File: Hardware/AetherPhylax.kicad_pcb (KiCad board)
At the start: 2 copper layers, 35 x 38 mm, 39 parts, among them J1 Conn_01x01_Pin, J2 Conn_01x01_Pin, U2 BME280, U3 STM32G071KxU, U4 RFM95W-868S2

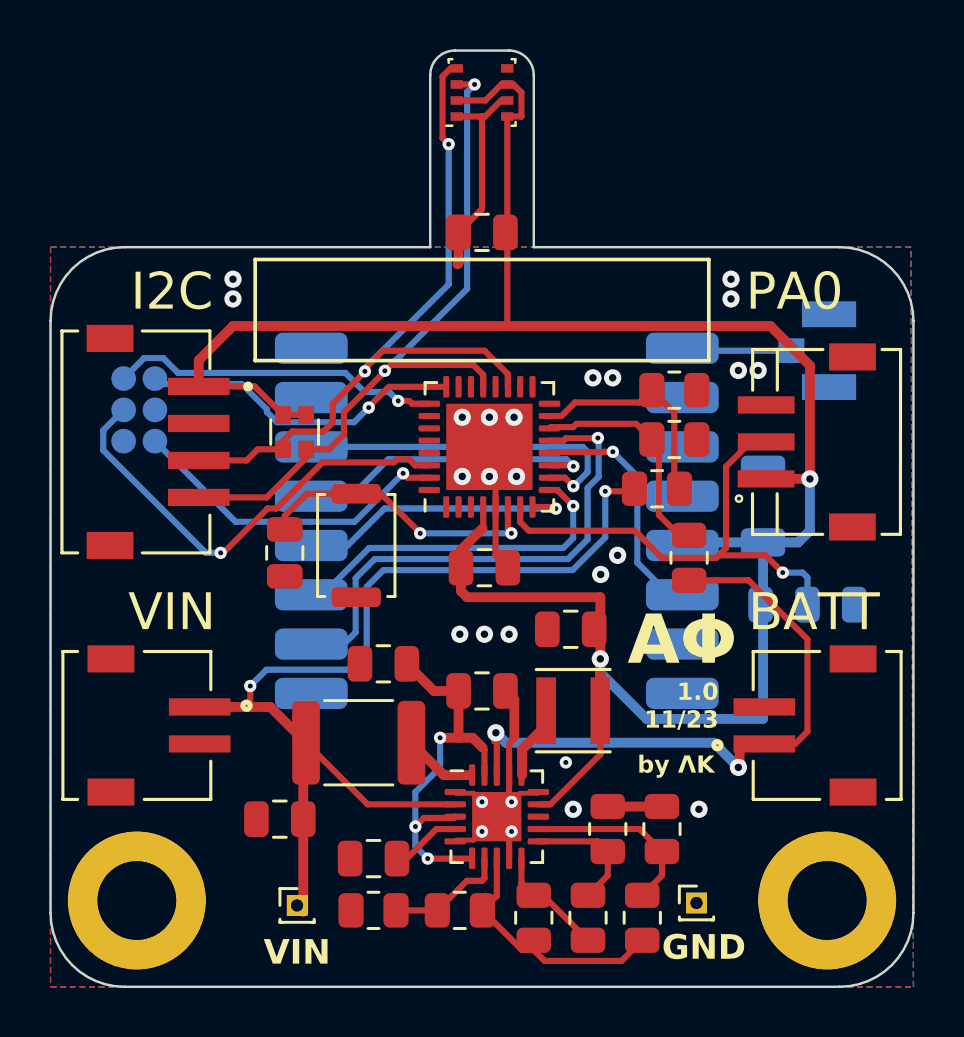
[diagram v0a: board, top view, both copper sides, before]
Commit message: switch to 4Layer Board, fixed I2C Addr
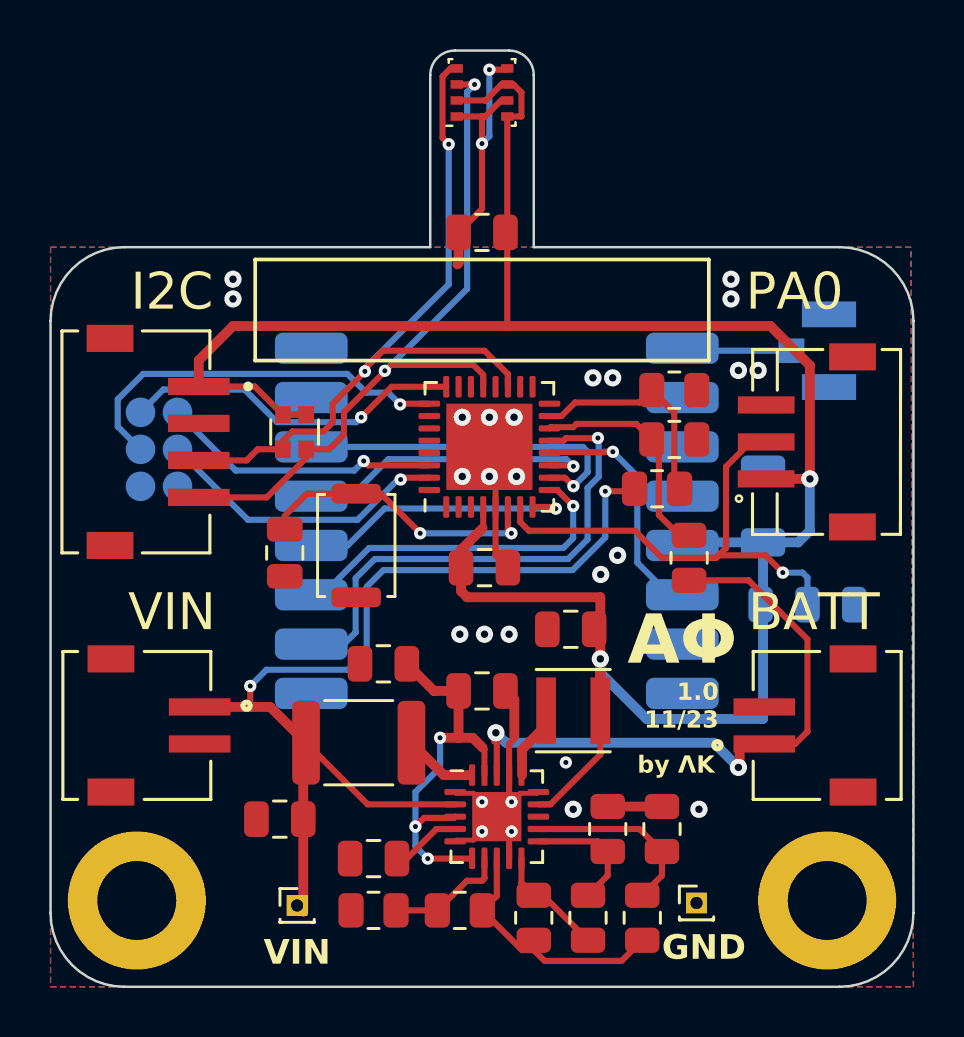
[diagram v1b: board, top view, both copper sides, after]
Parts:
- DEBUG1: value Conn_02x03_Top_Bottom -> Conn_02x03_Odd_Even; footprint Library:TestPoint_2x03_P1.27mm -> MyLib:TestPoint_2x03_1.5mm
- moved DEBUG1 1.79 mm to (139.4, 75.5)
- renumbered JP2 to JP1, R3 to R1, R4 to R2, R5 to R3, R6 to R4, ROK3 to ROK1, ROK1 to ROK3, ROUT2 to ROUT1, ROUT1 to ROUT2, ROV2 to ROV1, ROV1 to ROV2
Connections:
- DEBUG1 pad 2: SWCLK -> TX
- DEBUG1 pad 3: GND -> SWCLK
- DEBUG1 pad 4: TX -> RX
- DEBUG1 pad 5: RX -> GND
- U2 pad 5: unconnected-(U2-SDO-Pad5) -> GND
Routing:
- net TX: track 18.6 -> 11.4 mm
- net GND: track 26.6 -> 30.4 mm, vias 26 -> 28
- net SWCLK: track 13.5 -> 16.0 mm
- net RX: track 13.4 -> 12.1 mm
- net SWDIO: track 13.2 -> 13.9 mm
